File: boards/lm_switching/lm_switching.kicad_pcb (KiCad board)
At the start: 2 copper layers, 82.6 x 40.1 mm, 13 parts, among them J1 Conn_01x15, J2 Conn_01x15, SW1 SW_3PDT

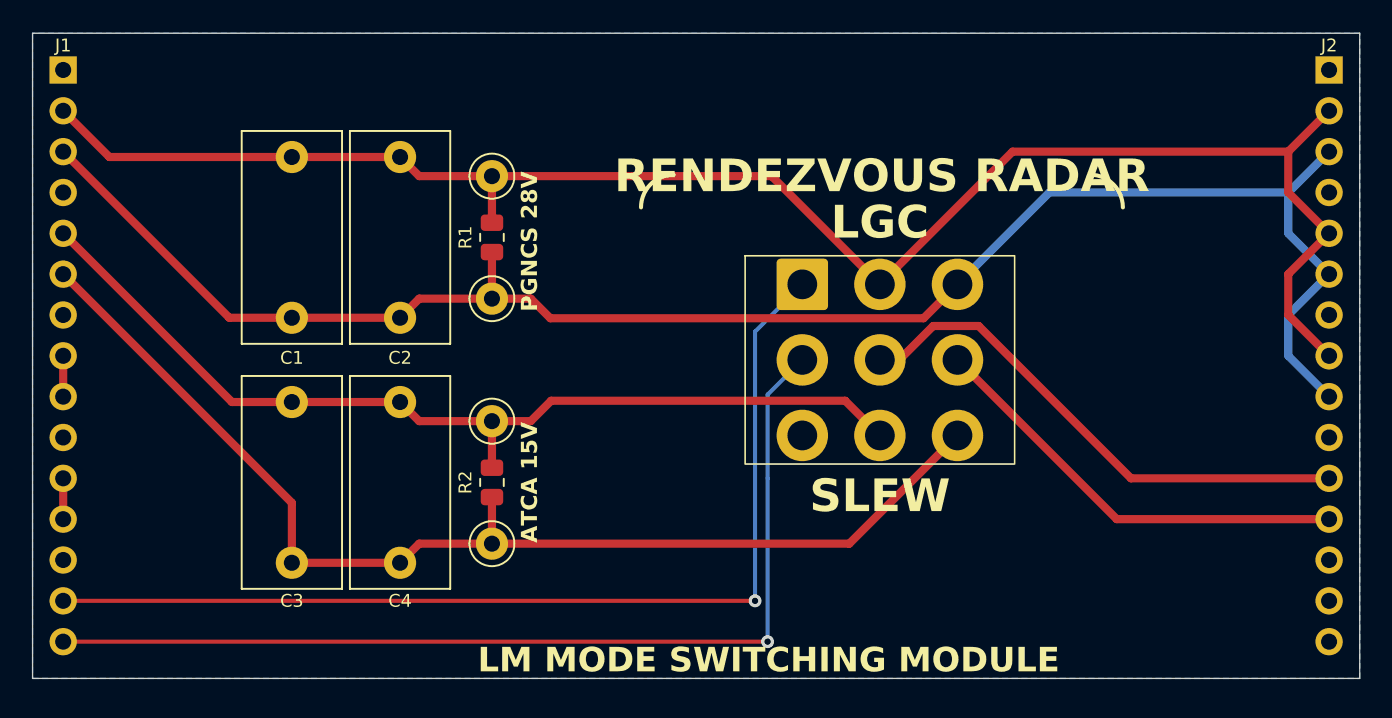
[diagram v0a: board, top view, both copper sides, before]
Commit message: Corrected switch layouts for auxiliary relays and LM switching boards
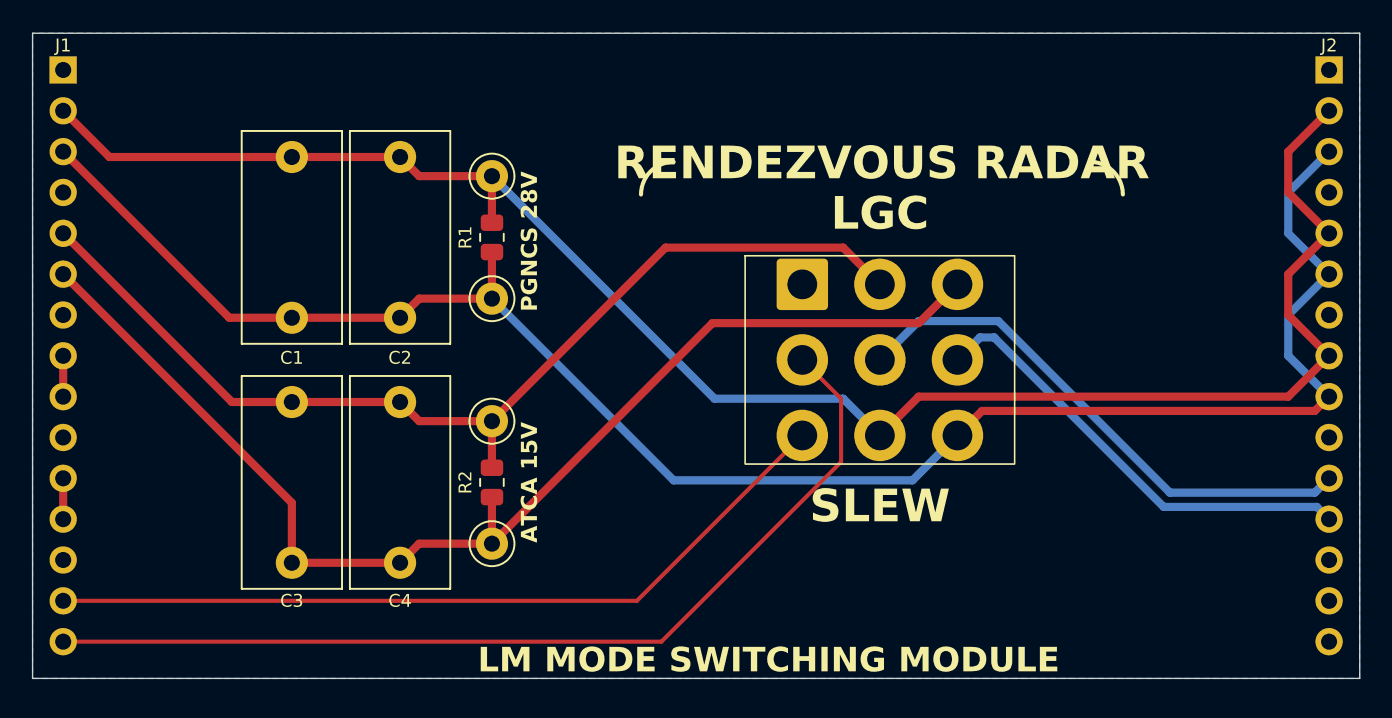
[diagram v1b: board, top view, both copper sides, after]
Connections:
- SW1 pad 1: /RD874 -> unconnected-(SW1-A-Pad1)
- SW1 pad 3: unconnected-(SW1-C-Pad3) -> /RD874
- SW1 pad 4: /PGNCS_800CPS_HI -> /ATCA_800CPS_HI
- SW1 pad 6: /ATCA_800CPS_HI -> /PGNCS_800CPS_HI
- SW1 pad 7: /PGNCS_800CPS_LO -> /ATCA_800CPS_LO
- SW1 pad 9: /ATCA_800CPS_LO -> /PGNCS_800CPS_LO
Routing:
- net /RD874: track 63.9 -> 50.2 mm, vias 1 -> 0
- net /PGNCS_800CPS_LO: track 107.1 -> 112.7 mm
- net /PGNCS_800CPS_HI: track 106.4 -> 111.5 mm
- net /ATCA_800CPS_HI: track 60.0 -> 64.0 mm
- net /ATCA_800CPS_LO: track 71.4 -> 75.3 mm
- net /RR_RES_REF_HI: track 32.7 -> 34.9 mm
- net /RRPONA: track 62.2 -> 60.4 mm, vias 1 -> 0
- net /RR_RES_REF_LO: track 27.2 -> 28.4 mm
